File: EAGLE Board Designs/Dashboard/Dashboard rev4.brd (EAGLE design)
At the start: 209.1 x 43.5 mm, 102 parts, among them J1 CONNECTOR-AVR-ISP_2X05_SMD, J2 CONNECTOR-6_μF_S_RA_, J3 CONNECTOR-CAN_μF_S_RA_, J4 CONNECTOR-8_μF_S_RA_, J5 JUMPER_0603_, Q1 TRANSISTOR_N_MOS__PMV15ENEA, Q2 TRANSISTOR_N_MOS__PMV15ENEA, Q3 TRANSISTOR_N_MOS__PMV15ENEA, Q4 TRANSISTOR_N_MOS__PMV15ENEA, Q5 TRANSISTOR_N_MOS__PMV15ENEA, Q6 TRANSISTOR_N_MOS__PMV15ENEA, Q7 TRANSISTOR_N_MOS__PMV15ENEA, Q8 TRANSISTOR_N_MOS__PMV15ENEA, U1 ATMEGA328P-AU, U2 RE46C100, U3 MCP23S08, U4 MCP2562FD, U5 MCP2515, X1 CRYSTAL_16MHZ, X2 CRYSTAL_16MHZ

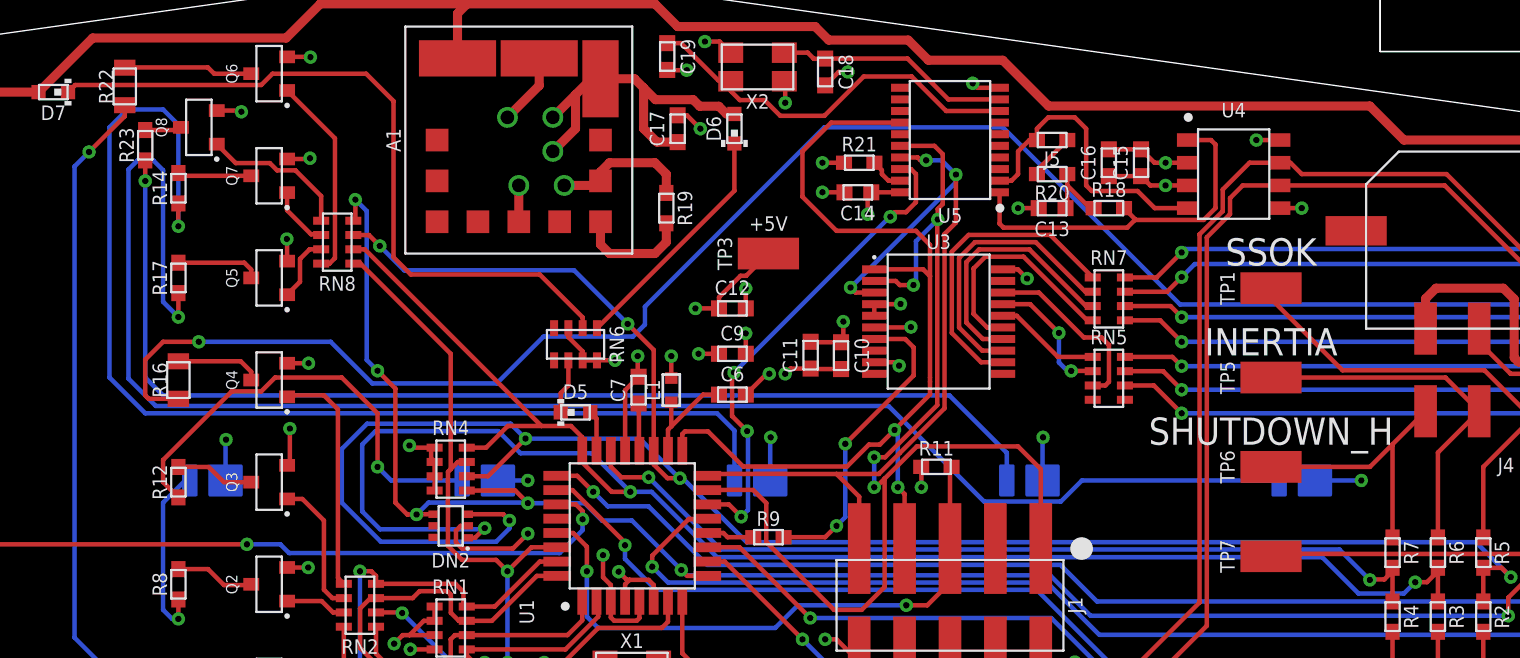
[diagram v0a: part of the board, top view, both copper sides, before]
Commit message: Updated routing and TP naming
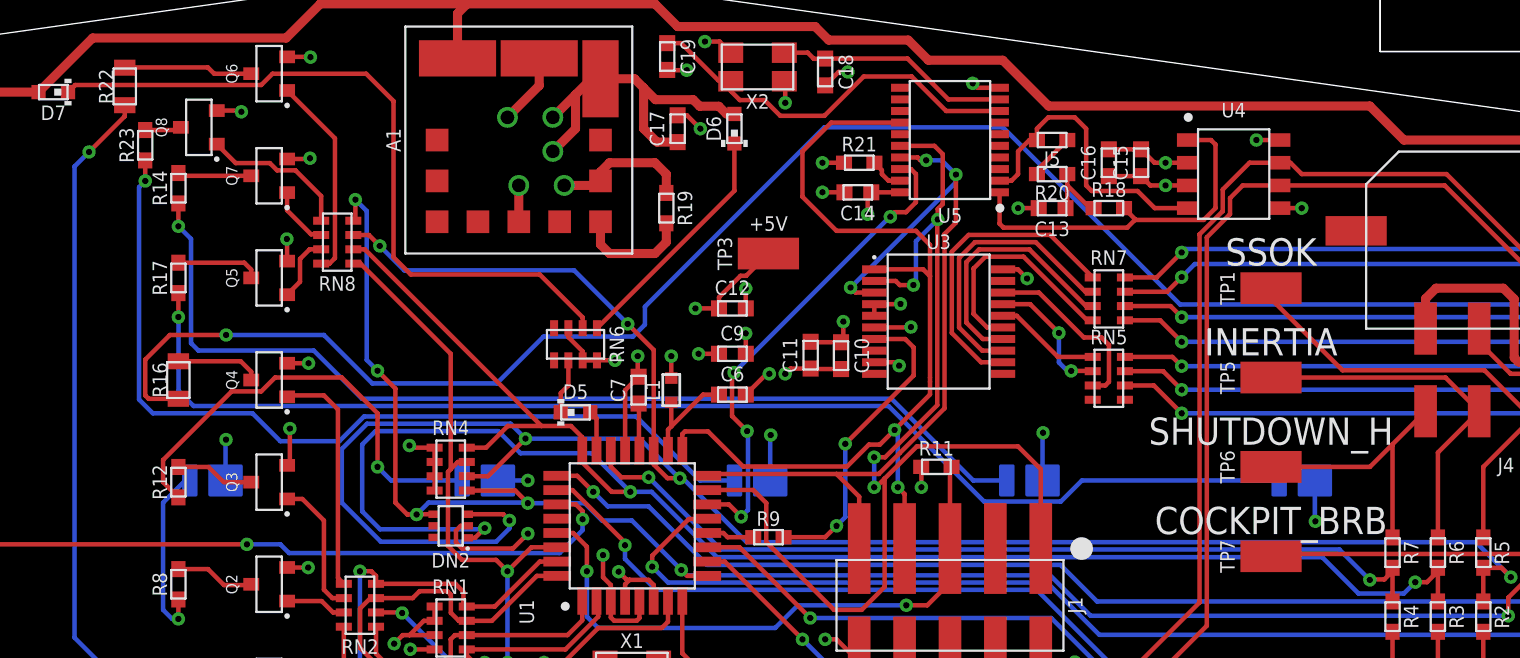
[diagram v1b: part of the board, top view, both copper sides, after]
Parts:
- D2: value LED_2835_GREEN -> LED_2835_AMBER
- moved D1 15.2 mm to (15.2, 15.2)
- moved D106 15.2 mm to (30.5, 15.2)
- renumbered D103 to D2
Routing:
- net N$40: track 91.7 -> 70.1 mm
- net N$20: track 63.7 -> 49.9 mm
- net N$49: track 64.6 -> 56.9 mm
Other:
- board text added: "COCKPIT_BRB"

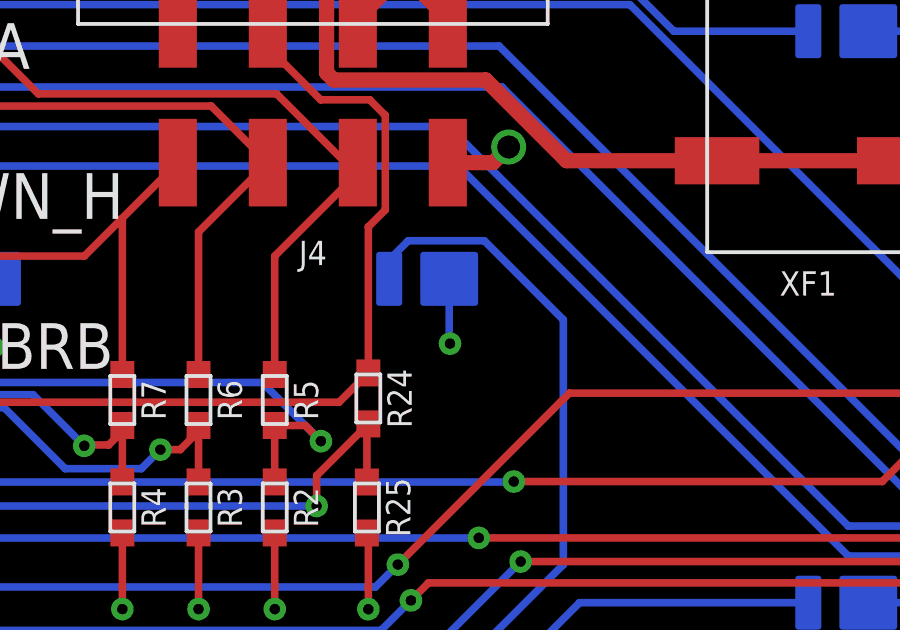
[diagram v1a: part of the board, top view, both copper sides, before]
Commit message: Added red-orange led for mcu led
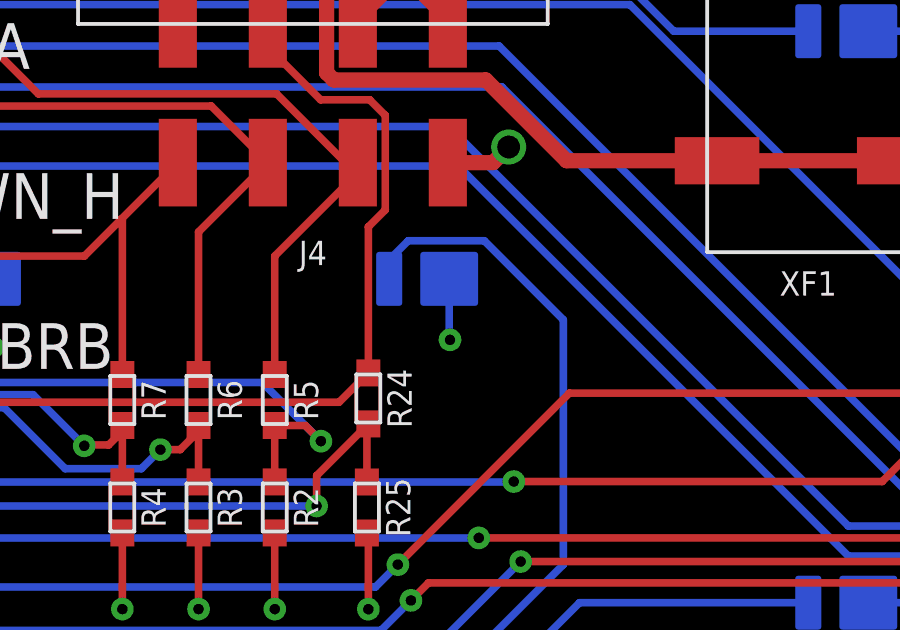
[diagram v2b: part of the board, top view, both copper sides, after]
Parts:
- D3: value LED_2835_AMBER -> LED_2835_RED-ORANGE
- renumbered D102 to D3
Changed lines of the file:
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@@
 <layer number="14" name="Route14" color="22" fill="1" visible="no" active="no"/>
 <layer number="15" name="Route15" color="23" fill="1" visible="no" active="yes"/>
-<layer number="16" name="Bottom" color="1" fill="1" visible="no" active="yes"/>
+<layer number="16" name="Bottom" color="1" fill="1" visible="yes" active="yes"/>
 <layer number="17" name="Pads" color="2" fill="1" visible="yes" active="yes"/>
 <layer number="18" name="Vias" color="2" fill="1" visible="yes" active="yes"/>
@@
 <layer number="22" name="bPlace" color="7" fill="1" visible="no" active="yes"/>
 <layer number="23" name="tOrigins" color="15" fill="1" visible="yes" active="yes"/>
-<layer number="24" name="bOrigins" color="15" fill="1" visible="no" active="yes"/>
+<layer number="24" name="bOrigins" color="15" fill="1" visible="yes" active="yes"/>
 <layer number="25" name="tNames" color="7" fill="1" visible="yes" active="yes"/>
 <layer number="26" name="bNames" color="7" fill="1" visible="no" active="yes"/>
@@
 <attribute name="VOLTAGE" value="50V" x="5.08" y="22.86" size="1.778" layer="27" rot="R180" display="off"/>
 </element>
-<element name="D102" library="HyTechDevices" package="2835-LED" value="LED_2835_AMBER" x="60.96" y="15.24" smashed="yes" rot="MR0">
-<attribute name="COLOR" value="Amber" x="60.96" y="15.24" size="1.778" layer="28" rot="MR0" display="off"/>
-<attribute name="DKPN" value="" x="60.96" y="15.24" size="1.778" layer="28" rot="MR0" display="off"/>
-<attribute name="MANUFACTURER" value="Lumileds" x="60.96" y="15.24" size="1.778" layer="28" rot="MR0" display="off"/>
-<attribute name="MOPN" value="997-L128PCA10350" x="60.96" y="15.24" size="1.778" layer="28" rot="MR0" display="off"/>
-<attribute name="MPN" value="L128-PCA1003500000" x="60.96" y="15.24" size="1.778" layer="28" rot="MR0" display="off"/>
-<attribute name="NAME" x="60.96" y="12.065" size="0.8128" layer="26" font="vector" rot="MR0" align="bottom-center"/>
-</element>
 <element name="C10" library="HyTechDevices" package="0603-CAP" value="CAPACITOR_0603_10V_0.1UF" x="19.939" y="22.225" smashed="yes" rot="R270">
 <attribute name="CAPACITANCE" value="0.1µF" x="19.939" y="21.209" size="1.778" layer="27" rot="R270" display="off"/>
@@
 </element>
 <element name="J1" library="HyTechDevices" package="2X05_SMD" value="CONNECTOR-AVR-ISP_2X05_SMD" x="26.035" y="8.255" smashed="yes" rot="R180">
-<attribute name="DKPN" value="S2011EC-03-ND" x="26.035" y="8.255" size="1.778" layer="27" rot="R180" display="off"/>
+<attribute name="DKPN" value="S2351E-05-ND" x="26.035" y="8.255" size="1.778" layer="27" rot="R180" display="off"/>
 <attribute name="MANUFACTURER" value="Sullins Connector Solutions" x="26.035" y="8.255" size="1.778" layer="27" rot="R180" display="off"/>
 <attribute name="MOPN" value="" x="26.035" y="8.255" size="1.778" layer="27" rot="R180" display="off"/>
-<attribute name="MPN" value="PRPC003DAAN-RC" x="26.035" y="8.255" size="1.778" layer="27" rot="R180" display="off"/>
+<attribute name="MPN" value="GBC05DABN-M30" x="26.035" y="8.255" size="1.778" layer="27" rot="R180" display="off"/>
 <attribute name="NAME" x="32.639" y="8.255" size="0.8128" layer="25" font="vector" rot="R270" align="bottom-center"/>
 </element>
@@
 <element name="XF1" library="HyTechDevices" package="3588" value="FUSE_HOLDER_MINIBLADESMD" x="73.66" y="24.13" smashed="yes" rot="R90">
 <attribute name="DKPN" value="36-3588-ND" x="73.66" y="24.13" size="1.778" layer="27" rot="R90" display="off"/>
+<attribute name="FUSE_TYPE" value="MINI 297" x="73.66" y="24.13" size="1.778" layer="27" rot="R90" display="off"/>
 <attribute name="MANUFACTURER" value="Keystone Electronics" x="73.66" y="24.13" size="1.778" layer="27" rot="R90" display="off"/>
 <attribute name="MOPN" value="534-3588" x="73.66" y="24.13" size="1.778" layer="27" rot="R90" display="off"/>
@@
 <attribute name="MPN" value="L128-PCA1003500000" x="45.72" y="15.24" size="1.778" layer="28" rot="MR0" display="off"/>
 <attribute name="NAME" x="45.72" y="17.526" size="0.8128" layer="26" font="vector" rot="MR0" align="bottom-center"/>
+</element>
+<element name="D3" library="HyTechDevices" package="2835-LED" value="LED_2835_RED-ORANGE" x="60.96" y="15.24" smashed="yes" rot="MR0">
+<attribute name="COLOR" value="Red-Orange" x="60.96" y="15.24" size="1.778" layer="28" rot="MR0" display="off"/>
+<attribute name="DKPN" value="" x="60.96" y="15.24" size="1.778" layer="28" rot="MR0" display="off"/>
+<attribute name="MANUFACTURER" value="Lumileds" x="60.96" y="15.24" size="1.778" layer="28" rot="MR0" display="off"/>
+<attribute name="MOPN" value="997-L128RNG10350 " x="60.96" y="15.24" size="1.778" layer="28" rot="MR0" display="off"/>
+<attribute name="MPN" value="L128-RNG1003500000 " x="60.96" y="15.24" size="1.778" layer="28" rot="MR0" display="off"/>
+<attribute name="NAME" x="60.96" y="17.526" size="0.8128" layer="26" font="vector" rot="MR0" align="bottom-center"/>
 </element>
 </elements>
@@
 <wire x1="75.665" y1="4.445" x2="77.4446" y2="4.445" width="0.254" layer="16"/>
 <wire x1="77.4446" y1="4.445" x2="77.5208" y2="4.3688" width="0.254" layer="16"/>
-<contactref element="D102" pad="A"/>
-<wire x1="61.695" y1="15.24" x2="61.695" y2="13.108" width="0.254" layer="16"/>
-<wire x1="61.722" y1="13.081" x2="61.695" y2="13.108" width="0.254" layer="16"/>
-<via x="61.722" y="13.081" extent="1-16" drill="0.35"/>
 <contactref element="D106" pad="A"/>
 <contactref element="D2" pad="A"/>
@@
 <wire x1="31.215" y1="17.88" x2="31.242" y2="17.907" width="0.254" layer="16"/>
 <via x="31.242" y="17.907" extent="1-16" drill="0.35"/>
+<contactref element="D3" pad="A"/>
+<wire x1="61.695" y1="15.24" x2="61.695" y2="13.235" width="0.254" layer="16"/>
+<wire x1="61.695" y1="13.235" x2="61.722" y2="13.208" width="0.254" layer="16"/>
+<via x="61.722" y="13.208" extent="1-16" drill="0.35"/>
 </signal>
 <signal name="CANL">
@@
 </signal>
 <signal name="N$2">
-<contactref element="D102" pad="C"/>
 <via x="-15.764" y="2.8608" extent="1-16" drill="0.35"/>
 <wire x1="-14.621" y1="2.8608" x2="-13.5128" y2="1.7526" width="0.254" layer="16"/>
@@
 <wire x1="62.865" y1="16.51" x2="65.5" y2="13.875" width="0.254" layer="16"/>
 <wire x1="62.865" y1="16.51" x2="60.33" y2="16.51" width="0.254" layer="16"/>
-<wire x1="60.33" y1="16.51" x2="59.695" y2="15.875" width="0.254" layer="16"/>
-<wire x1="59.695" y1="15.875" x2="59.695" y2="15.24" width="0.254" layer="16"/>
 <contactref element="R1" pad="1"/>
 <wire x1="-15.764" y1="2.8608" x2="-17.1408" y2="2.8608" width="0.254" layer="1"/>
@@
 <wire x1="-13.5128" y1="1.7526" x2="61.5376" y2="1.7526" width="0.254" layer="16"/>
 <wire x1="61.5376" y1="1.7526" x2="65.5" y2="5.715" width="0.254" layer="16"/>
+<contactref element="D3" pad="C"/>
+<wire x1="60.33" y1="16.51" x2="59.695" y2="15.875" width="0.254" layer="16"/>
+<wire x1="59.695" y1="15.875" x2="59.695" y2="15.24" width="0.254" layer="16"/>
 </signal>
 <signal name="N$4">

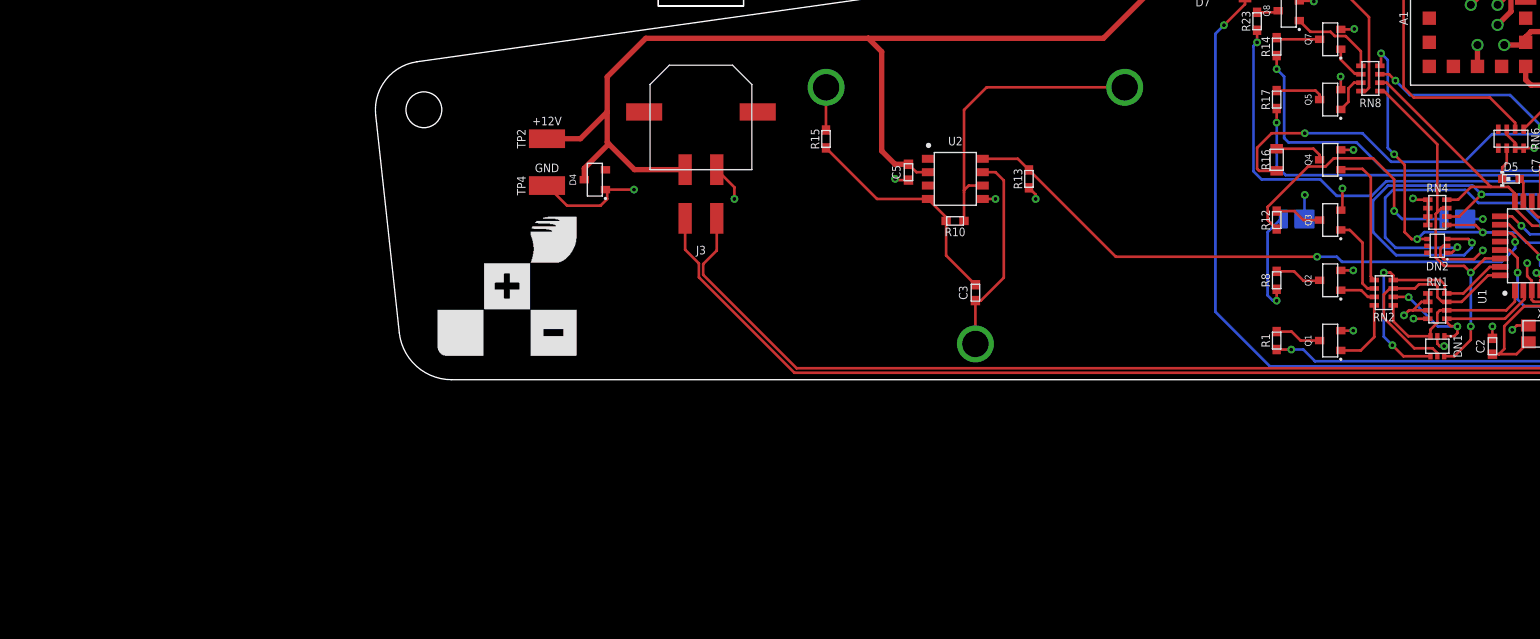
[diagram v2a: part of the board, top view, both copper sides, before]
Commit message: Added not gates and tractive LED
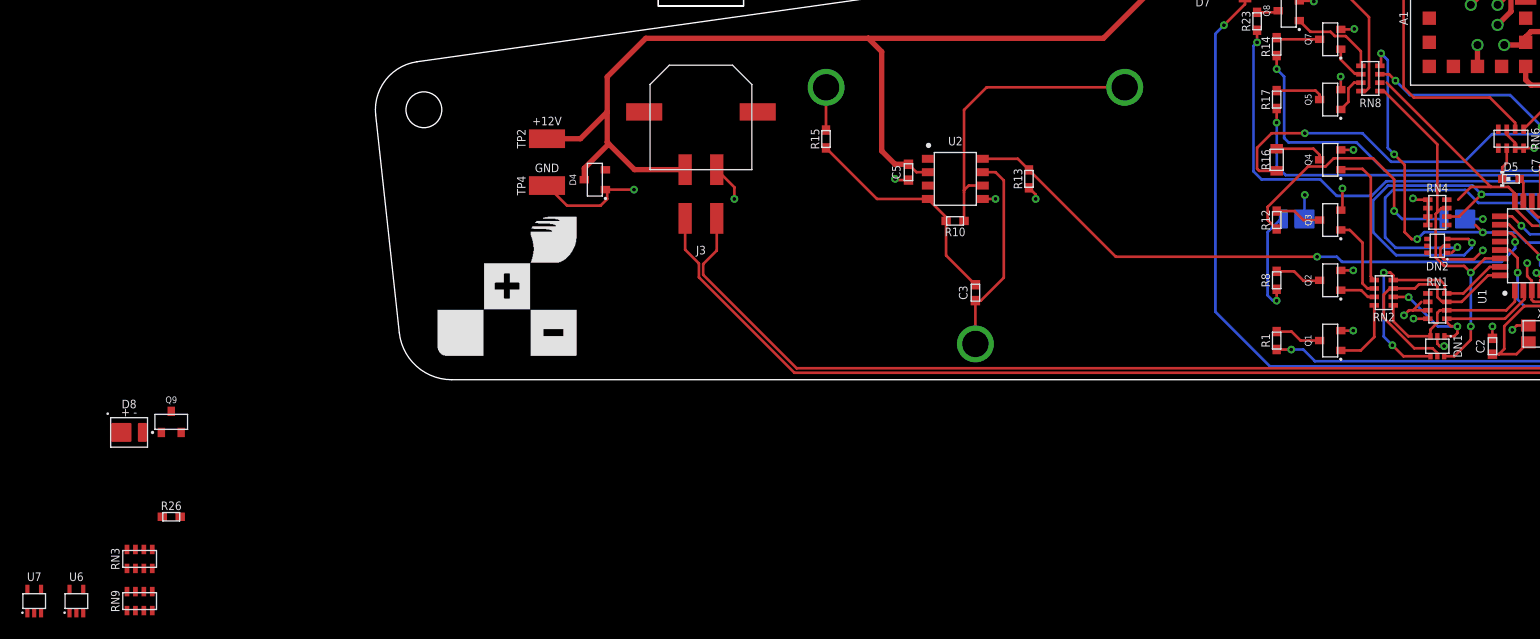
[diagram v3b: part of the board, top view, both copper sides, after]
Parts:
- added D8: LED_2835_GREEN, HyTechDevices:2835-LED
- added Q9: TRANSISTOR_N_MOS__PMV15ENEA, HyTechDevices:SOT-23
- added R26: RESISTOR_0603_15, HyTechDevices:0603-RES
- added RN3: RESISTOR_NETWORK_4_10K, HyTechDevices:1206-RES-ARRAY
- added RN9: RESISTOR_NETWORK_4_10, HyTechDevices:1206-RES-ARRAY
- added U6, U7: LOGICGATE_INVERTER_DCK3, HyTechDevices:SC-70-5
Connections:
- new net GND1: DN1.2, Q2.2, Q3.2, Q9.2, RN1.2, RN1.4, RN3.1
- new net LED_TRACTIVE: DN2.5, RN3.8, RN9.1, U1.28
- new net N$32: D104.A, D105.A, D8.A
- new net N$33: D8.C, R26.1
- new net N$45: Q9.3, R26.2
- new net N$47: Q9.1, RN9.8
- new net N$48: DN2.1, RN4.8, RN8.2, U6.4
- new net N$56: DN2.4, RN4.5, RN8.4, U7.4
- net +5V: now also U6.5, U7.5; no longer D104.A, D105.A
- net COCKPIT_BRB_READ: now also U7.2; no longer DN2.4, RN4.5, RN8.4
- net GND: now also U6.3, U7.3; no longer DN1.2, Q2.2, Q3.2, RN1.2, RN1.4
- net SHUTDOWN_G_READ: now also U6.2; no longer DN2.1, RN4.8, RN8.2
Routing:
- net GND: track 140.9 -> 133.3 mm, vias 52 -> 48
- net GND1: track 0.00 -> 6.12 mm, vias 0 -> 4
- net +5V: track 80.4 -> 76.4 mm, vias 26 -> 24
- net N$32: track 0.00 -> 3.98 mm, vias 0 -> 2
- net COCKPIT_BRB_READ: track 96.2 -> 92.4 mm
- net SHUTDOWN_G_READ: track 105.5 -> 103.4 mm

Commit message: ripup and reorder of leds
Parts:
- moved D8 127.6 mm to (0.00, 15.2), flipped to the bottom
- moved D104 17.3 mm to (-15.2, 23.5)
- moved D105 10.8 mm to (-15.2, 4.45)
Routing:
- net N$27: track 131.0 -> 0.00 mm, vias 1 -> 0
- net N$25: track 109.6 -> 0.00 mm, vias 1 -> 0
- net N$2: track 100.7 -> 0.63 mm, vias 1 -> 0
- net N$40: track 70.1 -> 0.00 mm, vias 1 -> 0
- net N$49: track 56.9 -> 0.00 mm, vias 1 -> 0
- net N$20: track 49.9 -> 0.00 mm, vias 1 -> 0
- net N$24: track 25.2 -> 0.00 mm, vias 1 -> 0
- net N$31: track 10.2 -> 0.00 mm, vias 1 -> 0
- net +5V: track 76.4 -> 66.8 mm, vias 24 -> 21
- net CS_CAN: track 27.5 -> 23.1 mm
- net N$32: track 3.98 -> 0.04 mm, vias 2 -> 1
- net N$17: track 92.5 -> 95.6 mm
- net N$16: track 94.8 -> 97.7 mm
- net N$19: track 65.1 -> 67.4 mm
- net N$18: track 67.2 -> 69.6 mm

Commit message: Began rewiring
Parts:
- removed RN3: RESISTOR_NETWORK_4_10K, HyTechDevices:1206-RES-ARRAY
- removed RN9: RESISTOR_NETWORK_4_10, HyTechDevices:1206-RES-ARRAY
- added R27: RESISTOR_0603_10, HyTechDevices:0603-RES
- added R28: RESISTOR_0603_10K, HyTechDevices:0603-RES
- moved U6 134.1 mm to (-5.00, 25.0), turned to 90 degrees
- moved U7 130.5 mm to (-9.00, 13.0), turned to 90 degrees
- moved Q9 99.3 mm to (-27.0, 25.0), turned to 90 degrees
- moved R26 96.2 mm to (-30.0, 15.0)
- moved D1 30.5 mm to (45.7, 15.2)
- moved D106 15.2 mm to (15.2, 15.2)
- moved D2 15.2 mm to (30.5, 15.2)
- moved Q1 6.00 mm to (-18.1, 3.71)
- moved Q2 6.00 mm to (-18.1, 9.43)
- moved Q3 6.00 mm to (-18.1, 15.1)
- moved Q4 6.00 mm to (-18.1, 20.9)
- moved Q5 6.00 mm to (-18.1, 26.6)
- moved Q6 6.00 mm to (-18.1, 38.0)
- moved Q7 6.00 mm to (-18.1, 32.3)
- moved D7 6.00 mm to (-30.1, 37.0)
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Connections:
- net GND1: now also R28.1; no longer RN3.1
- net LED_TRACTIVE: now also R27.1, R28.2; no longer RN3.8, RN9.1
- net N$47: now also R27.2; no longer RN9.8
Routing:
- net SHUTDOWN_G_READ: track 103.4 -> 25.0 mm, vias 3 -> 0
- net SHUTDOWN_F_READ: track 121.5 -> 139.5 mm
- net LED_MODE_CTRL: track 22.7 -> 34.7 mm
- net LED_IMD_CTRL: track 24.8 -> 36.8 mm
- net LED_START_CTRL: track 19.8 -> 25.8 mm
- net LED_MC_ERR_CTRL: track 17.0 -> 23.0 mm
- net LED_AMS_CTRL: track 36.2 -> 38.9 mm
- net COCKPIT_BRB_READ: track 92.4 -> 94.9 mm
- net STATUS_12V: track 40.6 -> 43.1 mm
- net GND: track 133.3 -> 131.1 mm
- net +12V: track 213.6 -> 214.8 mm
- net +5V: vias 21 -> 20
- net N$32: track 0.04 -> 0.00 mm, vias 1 -> 0
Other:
- board text added: "TSB"

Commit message: Working on reconnection
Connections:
- removed net GND1: DN1.2, Q2.2, Q3.2, Q9.2, R28.1, RN1.2, RN1.4
- net GND: now also DN1.2, Q2.2, Q3.2, Q9.2, R28.1, RN1.2, RN1.4
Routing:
- net N$27: track 0.00 -> 134.6 mm, vias 0 -> 1
- net N$2: track 0.63 -> 103.0 mm, vias 0 -> 1
- net N$25: track 0.00 -> 99.8 mm, vias 0 -> 1
- net N$20: track 0.00 -> 84.9 mm, vias 0 -> 1
- net N$40: track 0.00 -> 62.9 mm, vias 0 -> 1
- net N$49: track 0.00 -> 53.4 mm, vias 0 -> 1
- net N$24: track 0.00 -> 19.6 mm, vias 0 -> 1
- net N$31: track 0.00 -> 9.19 mm, vias 0 -> 1
- net GND1: track 6.12 -> 0.00 mm, vias 4 -> 0
- net GND: track 131.1 -> 137.0 mm, vias 48 -> 52
- net COCKPIT_BRB_READ: track 94.9 -> 94.1 mm
- net LED_AMS_CTRL: track 38.9 -> 39.5 mm
